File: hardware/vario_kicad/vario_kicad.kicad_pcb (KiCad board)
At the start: 2 copper layers, 85 parts, among them P1 USB_C_Plug_USB2.0, Q1 NMOS, Q2 PMOS, U2 BME280, U3 W25Q128JVS, U5 STM32L072CBTx, Y1 Crystal

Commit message: update usb c, minor other updates
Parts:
- removed P1: USB_C_Plug_USB2.0, symbol_lib:my_usbc
- added H1: MountingHole_Pad, MountingHole:MountingHole_2.2mm_M2_ISO7380_Pad, F.Cu at (103.0, 53.0)
- added H2: MountingHole_Pad, MountingHole:MountingHole_2.2mm_M2_ISO7380_Pad, F.Cu at (-30.2, 16.8)
- added H3: MountingHole_Pad, MountingHole:MountingHole_2.2mm_M2_ISO7380_Pad, F.Cu at (-30.2, 21.8)
- added H4: MountingHole_Pad, MountingHole:MountingHole_2.2mm_M2_ISO7380_Pad, F.Cu at (105.0, 105.0)
- added R15: 5k1, Resistor_SMD:R_0402_1005Metric, F.Cu at (-26.2, 12.2)
- added U4: USB C connector, symbol_lib:my_usbc, F.Cu at (-38.2, 9.95)
- BT2: footprint symbol_lib:lipo_footprint -> symbol_lib:battery_th
- moved D5 112.4 mm to (-38.2, 33.0)
- moved C14 112.1 mm to (-42.4, 28.3)
- moved C18 112.1 mm to (-42.4, 30.8)
- moved C19 112.1 mm to (-42.4, 33.3)
- moved U7 112.1 mm to (-37.8, 29.5)
- moved U8 104.6 mm to (-30.3, 31.8)
- moved TP10 99.6 mm to (-23.2, 13.8)
- moved TP9 99.6 mm to (-23.2, 10.7)
- moved C1 98.2 mm to (-48.7, 59.9)
- moved C10 98.2 mm to (-51.3, 23.0)
- moved C11 98.2 mm to (-76.2, 44.5)
- moved C15 98.2 mm to (-36.5, 61.6)
- moved C16 98.2 mm to (-36.5, 48.8)
- moved C17 98.2 mm to (-25.4, 48.8)
- moved C2 98.2 mm to (-48.7, 62.4)
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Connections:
- R4 pad 1: GND -> Net-(U4-CC2)
- R4 pad 2: Net-(P1-CC) -> GND
- U1 pad 9: (no net) -> GND

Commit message: v1 review of power
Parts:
- removed TP7, TP8: ~, TestPoint:TestPoint_Pad_D1.0mm
- added C12: 100nF, Capacitor_SMD:C_0603_1608Metric, F.Cu at (47.9, 66.8)
- moved H3 230.8 mm to (165.0, 145.0)
- moved S2 194.3 mm to (150.0, 105.0)
- moved H2 186.3 mm to (105.0, 145.0)
- moved R33 185.2 mm to (144.0, 105.0)
- moved S3 169.8 mm to (135.0, 105.0)
- moved S1 161.8 mm to (120.0, 105.0)
- moved TP11 130.6 mm to (55.5, 73.4)
- moved TP12 130.6 mm to (55.5, 76.5)
- moved C21 126.1 mm to (47.9, 69.3)
- moved C22 126.1 mm to (47.9, 71.8)
- moved C23 126.1 mm to (47.9, 74.3)
- moved C24 126.1 mm to (47.9, 76.8)
- moved C25 126.1 mm to (47.9, 79.4)
- moved Y1 125.7 mm to (59.2, 73.3)
- moved C11 125.7 mm to (47.9, 64.3)
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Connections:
- J2 pad 4: GND -> /mcu/NRST
- U4 pad S1: (no net) -> GND
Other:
- board outline added: 70 x 50 mm

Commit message: start layout
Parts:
- removed R33, R35: 100k, Resistor_SMD:R_0402_1005Metric
- removed R34: 1M, Resistor_SMD:R_0402_1005Metric
- removed S1, S2, S3: ~, symbol_lib:TS-1187A-B-A-B_switch
- added C13: 12.5pF, Capacitor_SMD:C_0402_1005Metric, F.Cu at (34.9, 88.7)
- added C20: 12.5pF, Capacitor_SMD:C_0402_1005Metric, F.Cu at (34.9, 90.7)
- added C28: 100nF, Capacitor_SMD:C_0603_1608Metric, F.Cu at (157.0, 141.5)
- added C29: 100nF, Capacitor_SMD:C_0603_1608Metric, F.Cu at (27.4, 97.7)
- added JP1: SolderJumper_2_Bridged, Jumper:SolderJumper-2_P1.3mm_Open_TrianglePad1.0x1.5mm, F.Cu at (38.5, 95.2)
- added JP2: SolderJumper_2_Bridged, Jumper:SolderJumper-2_P1.3mm_Open_TrianglePad1.0x1.5mm, B.Cu at (166.5, 117.7)
- added JP3: SolderJumper_2_Bridged, Jumper:SolderJumper-2_P1.3mm_Open_TrianglePad1.0x1.5mm, B.Cu at (158.7, 137.5)
- added R27: 100k, Resistor_SMD:R_0402_1005Metric, F.Cu at (127.0, 143.5)
- added R36: 100k, Resistor_SMD:R_0402_1005Metric, F.Cu at (142.0, 144.0)
- added R37: 100k, Resistor_SMD:R_0402_1005Metric, F.Cu at (157.0, 144.0)
- added R38: 100k, Resistor_SMD:R_0402_1005Metric, F.Cu at (125.5, 143.5)
- added R39: 100k, Resistor_SMD:R_0402_1005Metric, F.Cu at (140.5, 144.0)
- added R40: 100k, Resistor_SMD:R_0402_1005Metric, F.Cu at (155.5, 144.0)
- added S4: Switch, symbol_lib:TS-1187A-B-A-B_switch, F.Cu at (120.0, 142.0)
- added S5: Switch, symbol_lib:TS-1187A-B-A-B_switch, F.Cu at (135.0, 142.0)
- added S6: Switch, symbol_lib:TS-1187A-B-A-B_switch, F.Cu at (150.0, 142.0)
- added TP3: TestPoint, TestPoint:TestPoint_Pad_D1.0mm, F.Cu at (53.8, 59.5)
- added TP4: TestPoint, TestPoint:TestPoint_Pad_D1.0mm, F.Cu at (46.4, 77.9)
- added TP5: TestPoint, TestPoint:TestPoint_Pad_D1.0mm, F.Cu at (53.8, 62.6)
- added Y2: Crystal_GND24, Crystal:Crystal_SMD_3225-4Pin_3.2x2.5mm_HandSoldering, F.Cu at (39.7, 90.6)
- BT2, C14, C18, C19, Q1, Q2, R22, R23, R25, R29, U7, U8: moved to B.Cu
- C15: value 100n -> 1uF
- C16, C17: value 100n -> 100nF
- R10, R11, R8: value 10k -> 100k
- R24: value 100k -> 220k; moved to B.Cu
- R30: value 1M -> 0R
- R31: value 1M -> 0R; moved to B.Cu
- R32: value 100k -> 0R; moved to B.Cu
- TP1, TP2: value ~ -> TestPoint
- U1: footprint Package_SO:MSOP-8-1EP_3x3mm_P0.65mm_EP1.73x1.85mm -> Package_SO:MSOP-8-1EP_3x3mm_P0.65mm_EP2.5x3mm_Mask1.73x2.36mm
- moved C19 152.4 mm to (165.2, 138.5)
- moved C18 151.9 mm to (166.5, 131.0)
- moved C14 151.2 mm to (158.7, 145.5), turned to 180 degrees
- moved BT2 148.5 mm to (166.5, 125.0), turned to 90 degrees
- moved D5 145.8 mm to (167.0, 124.5), turned to 180 degrees
- moved U7 145.1 mm to (158.7, 142.1), turned to -90 degrees
- moved R22 140.8 mm to (163.5, 131.0)
- moved U8 140.3 mm to (165.3, 134.6), turned to 90 degrees
- moved R28 138.5 mm to (167.0, 126.0), turned to 180 degrees
- moved R29 135.6 mm to (155.5, 144.5), turned to -90 degrees
- moved R23 130.7 mm to (155.0, 127.5), turned to 90 degrees
- moved R24 130.1 mm to (153.0, 132.0), turned to 180 degrees
- moved Q1 127.9 mm to (159.0, 127.5)
- moved Q2 127.8 mm to (159.0, 132.0), turned to 180 degrees
- moved R25 127.8 mm to (152.5, 130.0), turned to 90 degrees
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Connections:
- BT2 pad 2: GND -> Net-(BT2--)
- C15 pad 1: /mcu/SW1 -> VCC
- C16 pad 1: /mcu/WKUP1 -> GND
- C16 pad 2: GND -> /mcu/SW1
- C17 pad 1: /mcu/SW3 -> GND
- C17 pad 2: GND -> /mcu/WKUP1
- R16 pad 1: VBATT_SW -> GND
- R30 pad 1: /mcu/SW1 -> Net-(JP1-A)
- R30 pad 2: GND -> /mcu/OSC_OUT
- R31 pad 1: /mcu/WKUP1 -> Net-(BT2--)
- R32 pad 1: VCC -> Net-(JP3-A)
- R32 pad 2: Net-(S1-A) -> VBATT
- R6 pad 1: /mcu/SPI1_MOSI -> /mcu/SPI1_MISO
- R7 pad 1: /mcu/SPI1_MISO -> /mcu/SPI1_MOSI
- U5 pad 2: unconnected-(U5-PC13-Pad2) -> /mcu/RTC_CALIB
- U5 pad 25: unconnected-(U5-PB12-Pad25) -> /leds/LED1
- U5 pad 29: /leds/LED1 -> unconnected-(U5-PA8-Pad29)
- U5 pad 5: unconnected-(U5-PH0-Pad5) -> /mcu/OSC_IN
- U5 pad 6: unconnected-(U5-PH1-Pad6) -> /mcu/OSC_OUT
- U7 pad 3: VBATT -> Net-(JP3-A)
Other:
- outline, holes or cut-outs redrawn
- rule pad_to_mask_clearance: 0 -> 0.05

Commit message: progress update on layout
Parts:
- removed TP1, TP10, TP2, TP3, TP5, TP9: TestPoint, TestPoint:TestPoint_Pad_D1.0mm
- C13, C20, C5, C6, C7, C8, C9, JP1, R16, R17, R18, R30, U1, Y2: moved to B.Cu
- moved C11 154.6 mm to (178.4, 47.2)
- moved C22 154.6 mm to (178.4, 54.7)
- moved C23 154.6 mm to (178.4, 57.2)
- moved C24 154.6 mm to (178.4, 59.7)
- moved C25 154.6 mm to (178.4, 62.2)
- moved C29 154.6 mm to (178.4, 64.7)
- moved TP11 154.6 mm to (197.4, 48.0)
- moved TP12 154.6 mm to (197.4, 51.0)
- moved U1 134.3 mm to (156.1, 115.4)
- moved C5 129.3 mm to (161.5, 116.3)
- moved C6 126.8 mm to (161.5, 114.4)
- moved R16 123.2 mm to (156.1, 118.1), turned to 180 degrees
- moved C7 116.9 mm to (149.5, 116.9), turned to 180 degrees
- moved R17 115.6 mm to (150.7, 114.6), turned to 180 degrees
- moved C4 114.1 mm to (128.0, 131.4), turned to -90 degrees
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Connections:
- U4 pad B6: unconnected-(U4-D+-PadB6) -> /mcu/USB_D+
- U4 pad B7: unconnected-(U4-D--PadB7) -> /mcu/USB_D-
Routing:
- net /mcu/USB_D-: track 0.00 -> 15.7 mm
- net /mcu/USB_D+: track 0.00 -> 15.4 mm

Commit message: layout close to done
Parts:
- removed TP11, TP12: TestPoint, TestPoint:TestPoint_Pad_D1.0mm
- moved C23 95.9 mm to (124.3, 136.4), turned to -90 degrees
- moved C24 92.8 mm to (126.2, 136.5), turned to -90 degrees
- moved C11 91.5 mm to (132.0, 126.0)
- moved C29 91.5 mm to (117.0, 132.5), turned to 90 degrees
- moved R7 91.2 mm to (135.8, 117.8), turned to 180 degrees
- moved R9 89.3 mm to (135.8, 116.3), turned to 180 degrees
- moved C22 89.0 mm to (120.9, 122.6)
- moved R11 86.2 mm to (134.9, 112.1), turned to -90 degrees
- moved C15 81.7 mm to (132.9, 110.9), turned to 90 degrees
- moved C3 80.6 mm to (131.0, 110.9), turned to 90 degrees
- moved R4 80.5 mm to (110.8, 127.5)
- moved C25 80.4 mm to (132.0, 127.8)
- moved R10 80.0 mm to (128.3, 111.3), turned to -90 degrees
- moved R8 79.6 mm to (126.6, 111.3), turned to -90 degrees
- moved U3 79.6 mm to (128.8, 115.9)
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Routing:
- net /mcu/USB_D-: track 15.7 -> 3.36 mm
- net /mcu/USB_D+: track 15.4 -> 3.84 mm
- net GND: track 0.00 -> 2.72 mm
- net /mcu/SPI1_MOSI: track 0.00 -> 1.15 mm

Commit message: asdf
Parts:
- C13, C20, JP1, R30, Y2: moved to F.Cu
- C26, C27, Y1: moved to B.Cu
- moved C20 47.6 mm to (135.7, 129.2), turned to 0 degrees
- moved C13 47.5 mm to (135.6, 137.2), turned to 180 degrees
- moved Y2 47.3 mm to (135.5, 133.1)
- moved R30 41.1 mm to (131.1, 133.7), turned to 180 degrees
- moved JP1 40.8 mm to (130.9, 131.7), turned to 180 degrees
- moved TP4 19.2 mm to (150.2, 136.3)
- moved C26 9.14 mm to (123.2, 131.4), turned to 180 degrees
- moved C27 9.14 mm to (123.2, 129.6), turned to 180 degrees
- moved Y1 4.94 mm to (125.3, 130.5)
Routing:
- net /mcu/OSC_IN: track 0.00 -> 17.0 mm
- net GND: track 2.72 -> 12.2 mm
- net Net-(JP1-A): track 0.00 -> 5.55 mm
- net /mcu/OSC_OUT: track 0.00 -> 3.83 mm

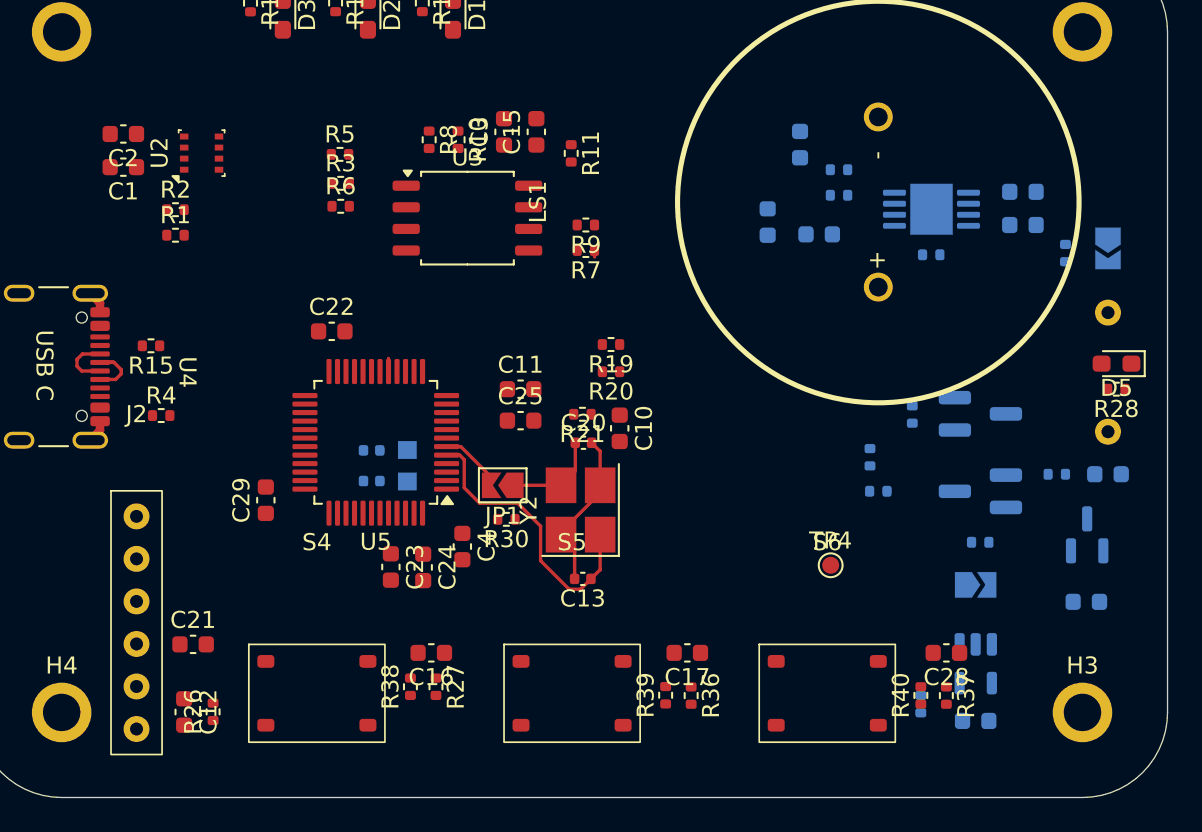
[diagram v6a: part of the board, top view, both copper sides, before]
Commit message: use 0402 instead of 0603 for almost all caps
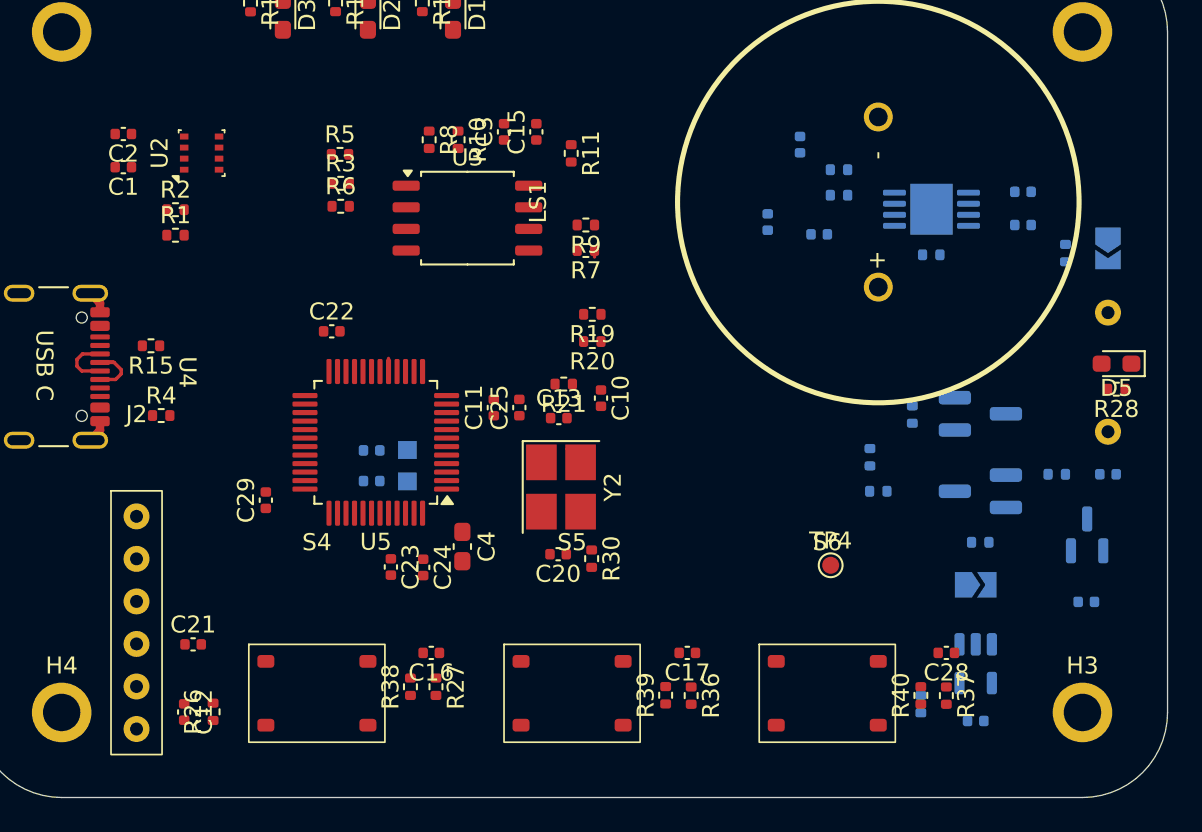
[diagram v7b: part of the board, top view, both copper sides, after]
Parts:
- removed JP1: SolderJumper_2_Bridged, Jumper:SolderJumper-2_P1.3mm_Open_TrianglePad1.0x1.5mm
- C1, C10, C11, C12, C14, C15, C16, C17, C18, C19, C2, C21, C22, C23, C24, C25, C28, C29, C3, C5, C6, C7, C8, C9: footprint Capacitor_SMD:C_0603_1608Metric -> Capacitor_SMD:C_0402_1005Metric
- C4: footprint Capacitor_SMD:C_0603_1608Metric -> Capacitor_SMD:C_0603_1608Metric_Pad1.08x0.95mm_HandSolder
- moved C13 9.55 mm to (134.2, 127.7), turned to 0 degrees
- moved C20 6.72 mm to (134.2, 135.7), turned to 180 degrees
- moved R30 5.52 mm to (136.2, 136.0), turned to -90 degrees
- moved C10 2.09 mm to (136.7, 126.5)
- moved R21 2.09 mm to (134.5, 125.7)
- moved R19 2.09 mm to (136.2, 121.6)
- moved R20 2.09 mm to (136.2, 123.2)
- moved C11 1.91 mm to (130.4, 127.1), turned to 90 degrees
- moved Y2 1.77 mm to (134.3, 131.8), turned to -90 degrees
- moved C25 0.77 mm to (131.9, 127.1), turned to 90 degrees
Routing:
- net /mcu/OSC_IN: track 17.0 -> 0.00 mm
- net GND: track 12.2 -> 4.45 mm
- net Net-(C20-Pad1): track 5.55 -> 0.00 mm
- net /mcu/OSC_OUT: track 3.83 -> 0.00 mm

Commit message: begin routing
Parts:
- C11, C23, C24, C25, C29, C4: moved to B.Cu
- moved C13 8.87 mm to (133.1, 136.5), turned to 180 degrees
- moved R30 8.55 mm to (130.9, 129.2), turned to 180 degrees
- moved C20 6.58 mm to (133.1, 129.2), turned to 0 degrees
- moved C25 1.99 mm to (130.1, 127.9), turned to -90 degrees
- moved Y2 1.60 mm to (133.2, 132.8), turned to 90 degrees
- moved C23 1.44 mm to (125.6, 135.7), turned to 180 degrees
- moved C11 1.38 mm to (131.5, 127.9), turned to -90 degrees
- moved C29 0.93 mm to (117.0, 131.6)
- moved C24 0.81 mm to (125.6, 136.9), turned to 180 degrees
- moved C4 0.42 mm to (128.4, 134.9)
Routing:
- net /mcu/OSC_IN: track 0.00 -> 9.98 mm
- net Net-(C20-Pad1): track 0.00 -> 3.70 mm
- net /mcu/OSC_OUT: track 0.00 -> 2.85 mm
- net GND: track 4.45 -> 6.95 mm
